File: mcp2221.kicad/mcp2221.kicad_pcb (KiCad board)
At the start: 2 copper layers, 47.2 x 34.6 mm, 25 parts, among them J1 Jumper 32 or 21, J2 Conn_01x04_Male, J3 Conn_01x03_Male, J4 Conn_01x06_Male, J5 Conn_01x03_Male, J6 Conn_01x06_Male, J7 Conn_01x02_Male, J8 Conn_01x02_Male, SW1 SW_Push, U1 AMS1117CD-3.3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

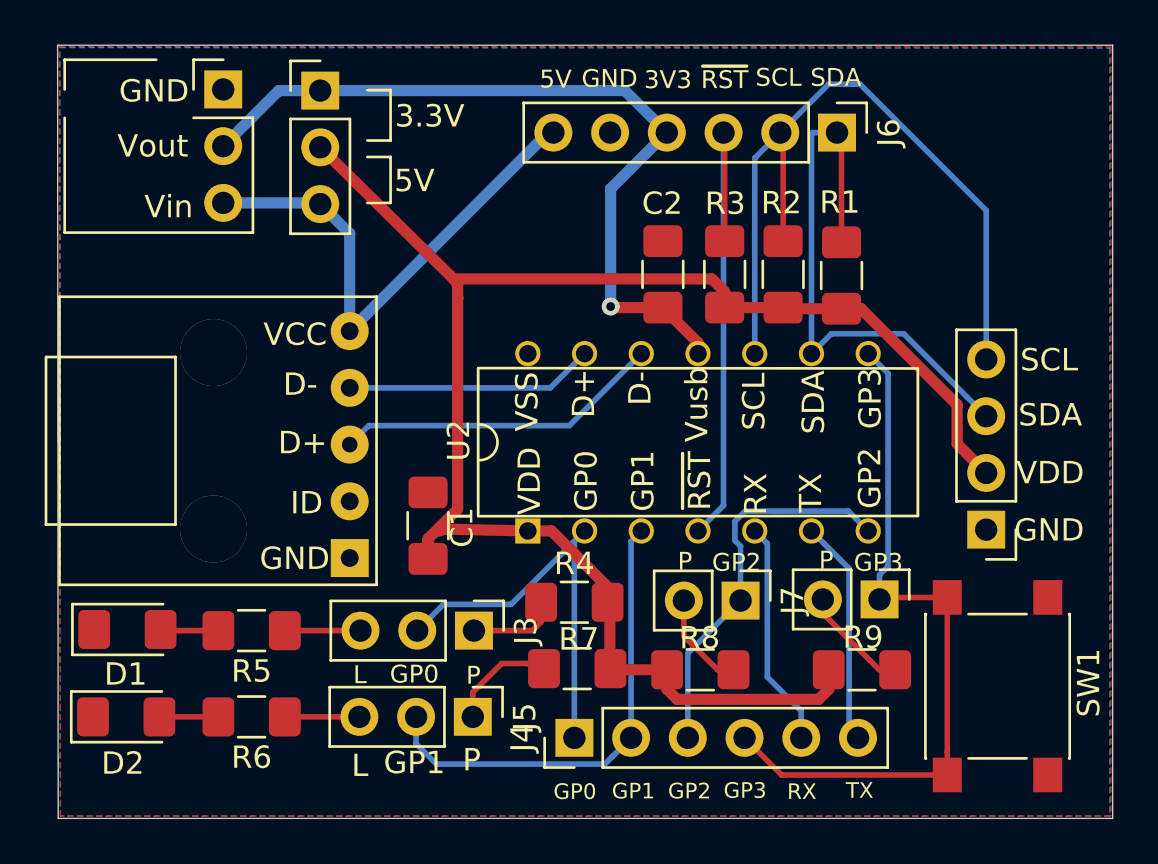
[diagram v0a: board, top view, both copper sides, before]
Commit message: make distance between connectors a multiple of 2.54 / optimize layout
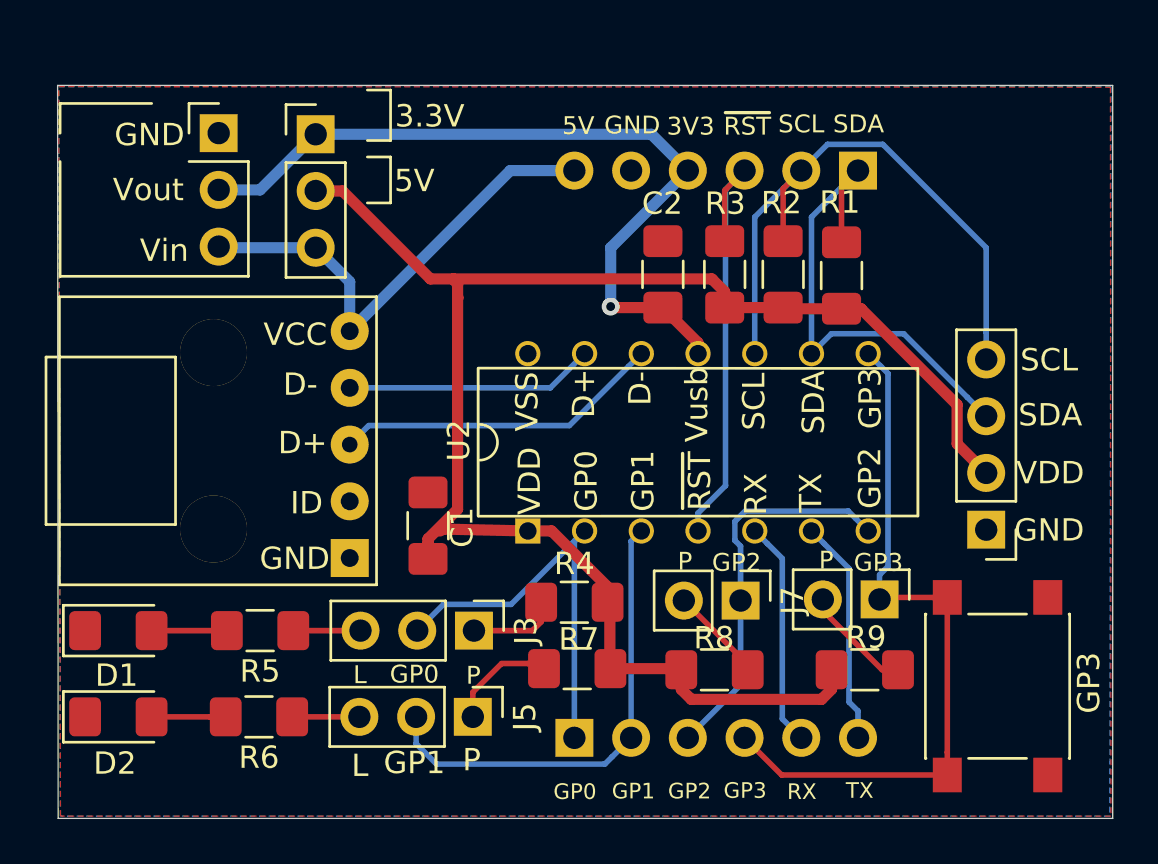
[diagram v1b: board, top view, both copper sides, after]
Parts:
- J4, J6: moved to B.Cu
- moved J1 1.97 mm to (75.8, 51.1)
- moved U1 1.97 mm to (71.5, 51.0)
- moved J6 1.94 mm to (100.1, 52.7), turned to 90 degrees
- moved R8 0.63 mm to (93.7, 75.0)
- moved D1 0.41 mm to (67.0, 73.3)
- moved R5 0.38 mm to (73.4, 73.3)
- moved D2 0.36 mm to (67.0, 77.1)
- moved R6 0.33 mm to (73.3, 77.1)
- moved R9 0.13 mm to (100.4, 75.0)
- turned J4 to 270 degrees
- renumbered SW1 to GP3
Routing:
- net /SCL: track 34.5 -> 28.2 mm
- net /SDA: track 25.8 -> 22.3 mm
- net /~RST~: track 23.3 -> 20.5 mm
- net /5V: track 23.3 -> 21.8 mm
- net Net-(D1-Pad2): track 2.61 -> 3.48 mm
- net Net-(D2-Pad2): track 2.64 -> 3.32 mm
- net Net-(J8-Pad2): track 4.91 -> 5.58 mm
- net /TX: track 10.1 -> 10.7 mm
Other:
- board size 47.2 x 34.6 mm -> 47.2 x 32.8 mm

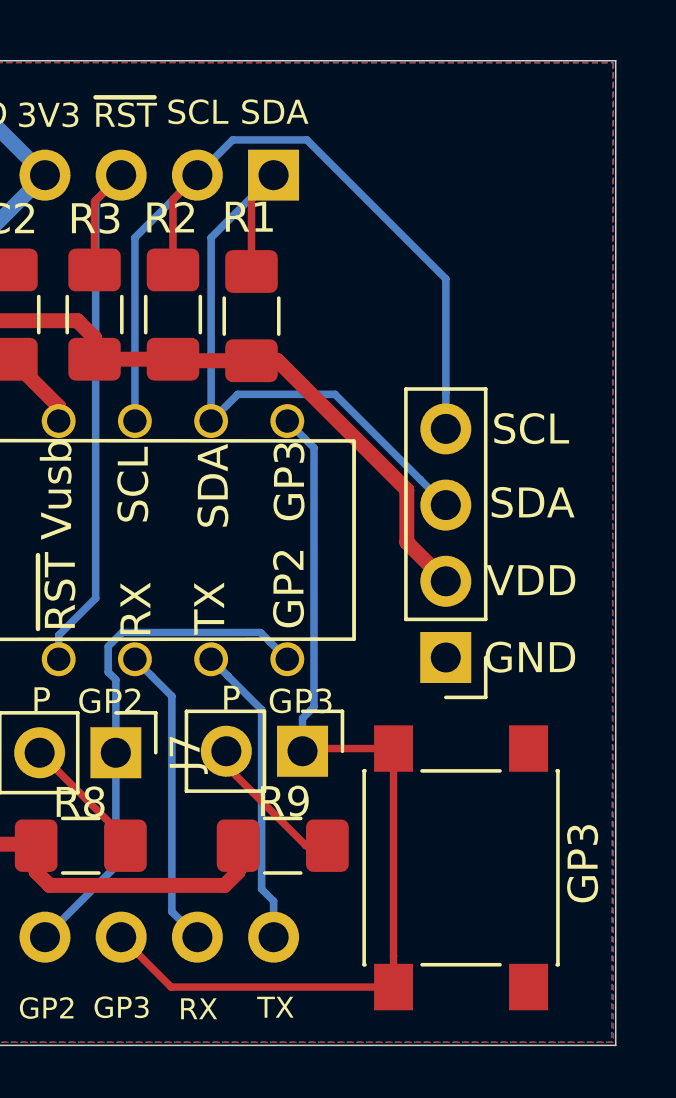
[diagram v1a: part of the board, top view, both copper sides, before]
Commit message: Rev 7: added button for GP2
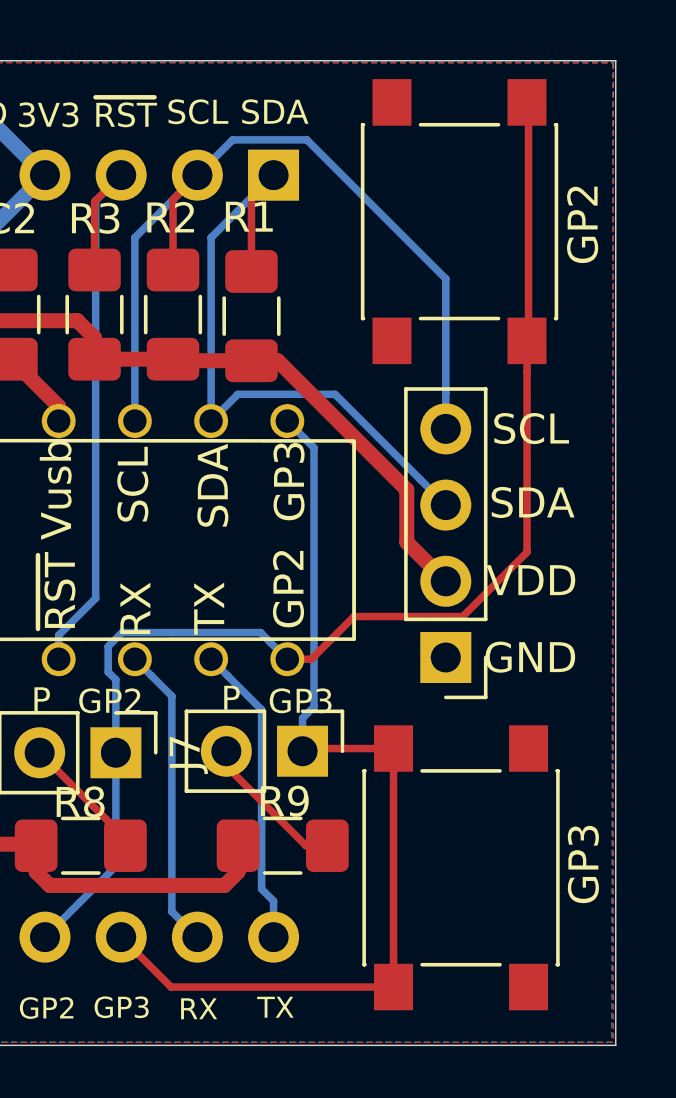
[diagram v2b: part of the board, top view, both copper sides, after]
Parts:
- added SW2: SW_Push, Button_Switch_SMD:SW_Push_1P1T_NO_6x6mm_H9.5mm, F.Cu at (106.3, 54.2)
- renumbered GP3 to SW1
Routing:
- net /GP2: track 17.3 -> 41.8 mm
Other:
- board text added: "Rev 7"
- board text removed: "Rev 6"
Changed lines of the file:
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@@
   (general
     (thickness 1.6)
-    (drawings 41)
-    (tracks 143)
+    (drawings 43)
+    (tracks 150)
     (zones 0)
-    (modules 25)
+    (modules 26)
     (nets 25)
   )
@@
     (add_net /VDD)
   )
+  (module Button_Switch_SMD:SW_Push_1P1T_NO_6x6mm_H9.5mm (layer F.Cu)
+    (at 106.3244 54.229 270)
+    (descr "tactile push button, 6x6mm e.g. PTS645xx series, height=9.5mm")
+    (tags "tact sw push 6mm smd")
+    (attr smd)
+    (fp_text reference SW2 (at 0 -4.05 90) (layer F.SilkS) hide
+      (effects (font (size 1 1) (thickness 0.15)))
+    )
+    (fp_text value SW_Push (at 0 4.15 90) (layer F.Fab)
+      (effects (font (size 1 1) (thickness 0.15)))
+    )
+    (fp_circle (center 0 0) (end 1.75 -0.05) (layer F.Fab) (width 0.1))
+    (fp_line (start -3.23 3.23) (end 3.23 3.23) (layer F.SilkS) (width 0.12))
+    (fp_line (start -3.23 -1.3) (end -3.23 1.3) (layer F.SilkS) (width 0.12))
+    (fp_line (start -3.23 -3.23) (end 3.23 -3.23) (layer F.SilkS) (width 0.12))
+    (fp_line (start 3.23 -1.3) (end 3.23 1.3) (layer F.SilkS) (width 0.12))
+    (fp_line (start -3.23 -3.2) (end -3.23 -3.23) (layer F.SilkS) (width 0.12))
+    (fp_line (start -3.23 3.23) (end -3.23 3.2) (layer F.SilkS) (width 0.12))
+    (fp_line (start 3.23 3.23) (end 3.23 3.2) (layer F.SilkS) (width 0.12))
+    (fp_line (start 3.23 -3.23) (end 3.23 -3.2) (layer F.SilkS) (width 0.12))
+    (fp_line (start -5 -3.25) (end 5 -3.25) (layer F.CrtYd) (width 0.05))
+    (fp_line (start -5 3.25) (end 5 3.25) (layer F.CrtYd) (width 0.05))
+    (fp_line (start -5 -3.25) (end -5 3.25) (layer F.CrtYd) (width 0.05))
+    (fp_line (start 5 3.25) (end 5 -3.25) (layer F.CrtYd) (width 0.05))
+    (fp_line (start 3 -3) (end -3 -3) (layer F.Fab) (width 0.1))
+    (fp_line (start 3 3) (end 3 -3) (layer F.Fab) (width 0.1))
+    (fp_line (start -3 3) (end 3 3) (layer F.Fab) (width 0.1))
+    (fp_line (start -3 -3) (end -3 3) (layer F.Fab) (width 0.1))
+    (fp_text user %R (at 0 -4.05 90) (layer F.Fab)
+      (effects (font (size 1 1) (thickness 0.15)))
+    )
+    (pad 2 smd rect (at 3.975 2.25 270) (size 1.55 1.3) (layers F.Cu F.Paste F.Mask)
+      (net 1 GND))
+    (pad 1 smd rect (at 3.975 -2.25 270) (size 1.55 1.3) (layers F.Cu F.Paste F.Mask)
+      (net 9 /GP2))
+    (pad 1 smd rect (at -3.975 -2.25 270) (size 1.55 1.3) (layers F.Cu F.Paste F.Mask)
+      (net 9 /GP2))
+    (pad 2 smd rect (at -3.975 2.25 270) (size 1.55 1.3) (layers F.Cu F.Paste F.Mask)
+      (net 1 GND))
+    (model ${KISYS3DMOD}/Button_Switch_SMD.3dshapes/SW_PUSH_6mm_H9.5mm.wrl
+      (at (xyz 0 0 0))
+      (scale (xyz 1 1 1))
+      (rotate (xyz 0 0 0))
+    )
+  )
   (module user:AMS1117_Breakout (layer F.Cu)
     (at 71.501 51.0032)
@@
     (tags "tact sw push 6mm smd")
     (attr smd)
-    (fp_text reference GP3 (at 0.1524 4.0894 90) (layer F.SilkS)
+    (fp_text reference SW1 (at 0.1524 4.0894 90) (layer F.SilkS) hide
       (effects (font (size 1 1) (thickness 0.15)))
     )
@@
       (net 1 GND))
   )
+  (gr_text GP2 (at 110.4646 54.3052 90) (layer F.SilkS)
+    (effects (font (size 1 1) (thickness 0.15)))
+  )
+  (gr_text GP3 (at 110.49 75.6412 90) (layer F.SilkS)
+    (effects (font (size 1 1) (thickness 0.15)))
+  )
   (gr_text GP3 (at 101.0412 70.231) (layer F.SilkS)
     (effects (font (size 0.8 0.8) (thickness 0.15)))
@@
     (effects (font (size 0.8 0.8) (thickness 0.15)))
   )
-  (gr_text "Rev 6" (at 67.7926 80.2894) (layer B.SilkS)
+  (gr_text "Rev 7" (at 67.7926 80.2894) (layer B.SilkS)
     (effects (font (size 1 1) (thickness 0.15)) (justify mirror))
   )
@@
   (segment (start 94.869 75.7174) (end 94.869 71.9328) (width 0.25) (layer B.Cu) (net 9))
   (segment (start 92.5068 78.0796) (end 94.869 75.7174) (width 0.25) (layer B.Cu) (net 9))
+  (segment (start 108.6252 58.3818) (end 108.6252 50.4318) (width 0.25) (layer F.Cu) (net 9))
+  (segment (start 102.806429 67.392801) (end 106.431201 67.392801) (width 0.25) (layer F.Cu) (net 9))
+  (segment (start 108.5744 65.249602) (end 108.5744 59.229) (width 0.25) (layer F.Cu) (net 9))
+  (segment (start 106.431201 67.392801) (end 108.5744 65.249602) (width 0.25) (layer F.Cu) (net 9))
+  (segment (start 101.38303 68.8162) (end 102.806429 67.392801) (width 0.25) (layer F.Cu) (net 9))
+  (segment (start 108.5744 59.229) (end 108.5744 58.204) (width 0.25) (layer F.Cu) (net 9))
+  (segment (start 100.584 68.8162) (end 101.38303 68.8162) (width 0.25) (layer F.Cu) (net 9))
   (segment (start 89.9668 69.2734) (end 90.424 68.8162) (width 0.25) (layer B.Cu) (net 10))
   (segment (start 89.9668 78.0796) (end 89.9668 69.2734) (width 0.25) (layer B.Cu) (net 10))
